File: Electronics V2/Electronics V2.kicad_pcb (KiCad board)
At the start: 2 copper layers, 102 x 62 mm, 88 parts, among them J1 MOT_L, J2 MOT_R, J3 SD_Card, J4 USB_C_Receptacle_USB2.0_14P, J5 Power Probes, J6 L1, J7 L2, Q1 BC547, SW1 BTN_0, SW2 MSTP_SEL, SW3 RST, SW4 BOOT, SW5 BTN_1, SW6 BTN_2, SW7 BTN_3, SW8 INCR_0, U1 NCP1117-3.3_SOT223, U10 TVS1400DRV, U11 TVS1400DRV, U2 TMC2209, U3 ESP32-S3-WROOM-1, U4 DAC081C081CIMK, U5 IMU_L, U6 IMU_R, U7 NCP1117-3.3_SOT223, U8 SSD1036, U9 TMC2209

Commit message: completed pcb fr this time
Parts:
- removed the U5 at (108.6, 78.3)
- added U5: IMU_L, Package_LGA:Bosch_LGA-14_3x2.5mm_P0.5mm, F.Cu at (112.7, 92.5)
- added U5: IMU_L, Package_LGA:Bosch_LGA-14_3x2.5mm_P0.5mm, F.Cu at (199.8, 104.2)
- moved U6 52.6 mm to (150.8, 104.4), turned to -90 degrees
- moved 10k 6.82 mm to (194.5, 75.9), turned to 0 degrees
- moved 10n 3.91 mm to (194.5, 74.4), turned to 180 degrees
- moved J4 2.51 mm to (199.7, 113.0)
- moved 10k 1.49 mm to (194.5, 72.9), turned to 180 degrees
- moved J3 0.41 mm to (117.0, 99.6)
- moved 100n 0.38 mm to (158.9, 121.7)
- moved 1k 0.38 mm to (158.8, 119.9)
- moved D1 0.38 mm to (158.9, 118.2)
- moved 10k 0.30 mm to (146.2, 81.0)
- moved 100n 0.18 mm to (197.5, 80.8)
- moved 100n 0.15 mm to (197.5, 82.3)
- moved 10k 0.10 mm to (149.6, 81.0)
- renumbered R24 to 1.5k, C3 to 100n, C11 to 100n, C24 to 100n, C6 to 100n, C17 to 100n, C14 to 100n, C13 to 100n, C5 to 100n, C16 to 100n, C12 to 100n, C7 to 100n, C1 to 100n, C18 to 100n, C10 to 100n, C23 to 100n, C2 to 100n, C4 to 100u, R2 to 10k, R19 to 10k, R1 to 10k, R15 to 10k, R14 to 10k, R9 to 10k, R11 to 10k, R6 to 10k, R16 to 10k, R26 to 10k, R18 to 10k, R25 to 10k, R17 to 10k, R13 to 10k, R7 to 10k, R3 to 10k, R10 to 10k, C26 to 10n, C27 to 10n, C22 to 10u, C19 to 10u, C21 to 10u, C20 to 10u, R23 to 1k, R12 to 1k, R21 to 1k, R22 to 1k, C8 to 22n, C25 to 22n, R8 to 330m, R4 to 330m, R20 to 330m, R5 to 330m, U9 to TMC2209
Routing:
- net GND: track 51.3 -> 9.29 mm, vias 16 -> 0
- net /SCL: track 163.6 -> 140.9 mm, vias 8 -> 7
- net /SDA: track 155.4 -> 141.2 mm, vias 6 -> 7
- net /MISO: track 10.8 -> 4.26 mm
- net Net-(C26-Pad1): track 5.40 -> 9.37 mm
- net /D+: track 46.2 -> 43.7 mm
- net /D-: track 46.2 -> 43.7 mm
- net /VREF: track 53.3 -> 51.3 mm
- net Net-(C27-Pad1): track 12.0 -> 10.5 mm, vias 2 -> 0
- net /CS_SD: track 31.4 -> 32.8 mm
- net +5V: track 211.1 -> 209.9 mm
- net /SCLK: track 13.6 -> 14.7 mm
- net /~{EN}: track 68.5 -> 67.5 mm
- net /MOSI: track 28.0 -> 27.1 mm
- net /DIR_L: track 37.5 -> 36.6 mm
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- removed copper zone on B.Cu, net GND
- removed copper zone on F.Cu, net GND

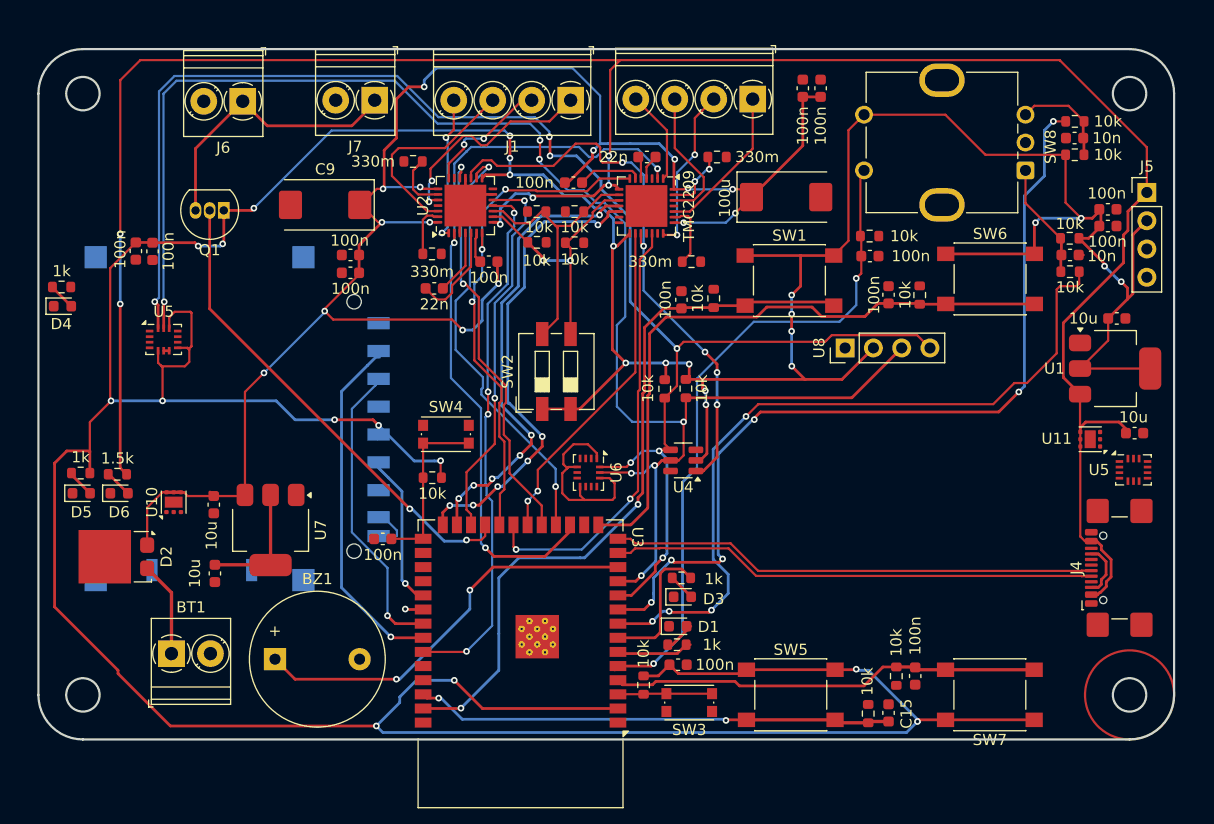
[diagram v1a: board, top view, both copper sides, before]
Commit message: added copper fill
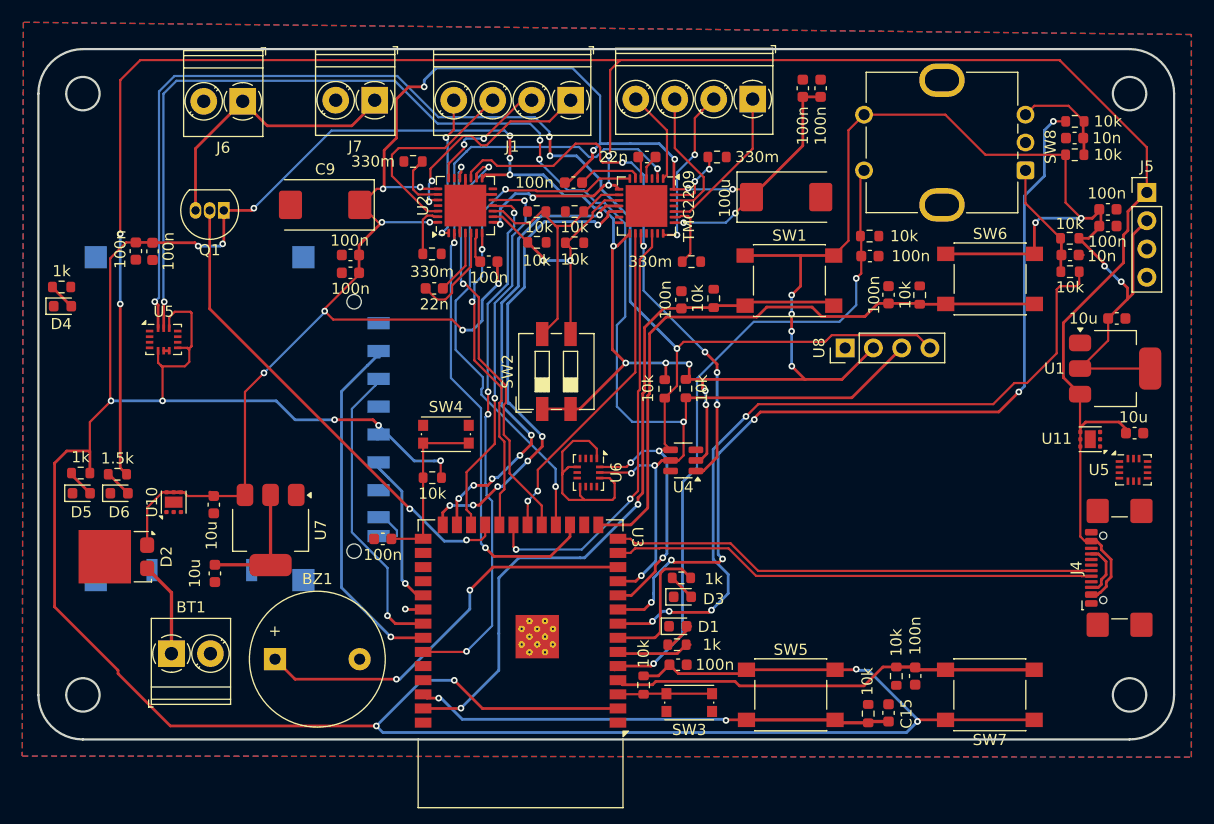
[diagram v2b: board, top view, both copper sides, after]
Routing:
- net +3V3: track 482.3 -> 483.7 mm
- added copper zone on B.Cu, net GND
- added copper zone on F.Cu, net GND

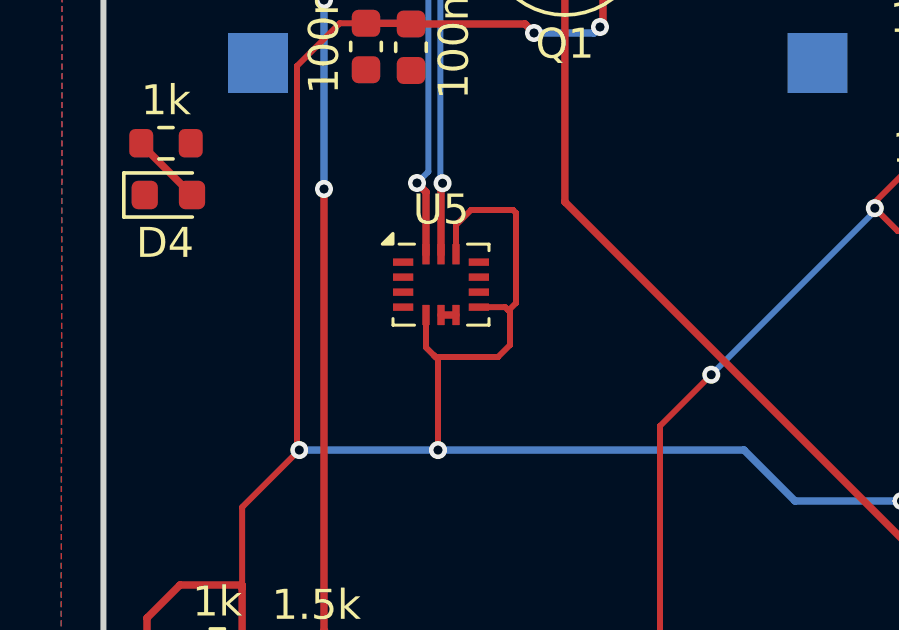
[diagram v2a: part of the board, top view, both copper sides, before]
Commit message: added copper fill + cleaning
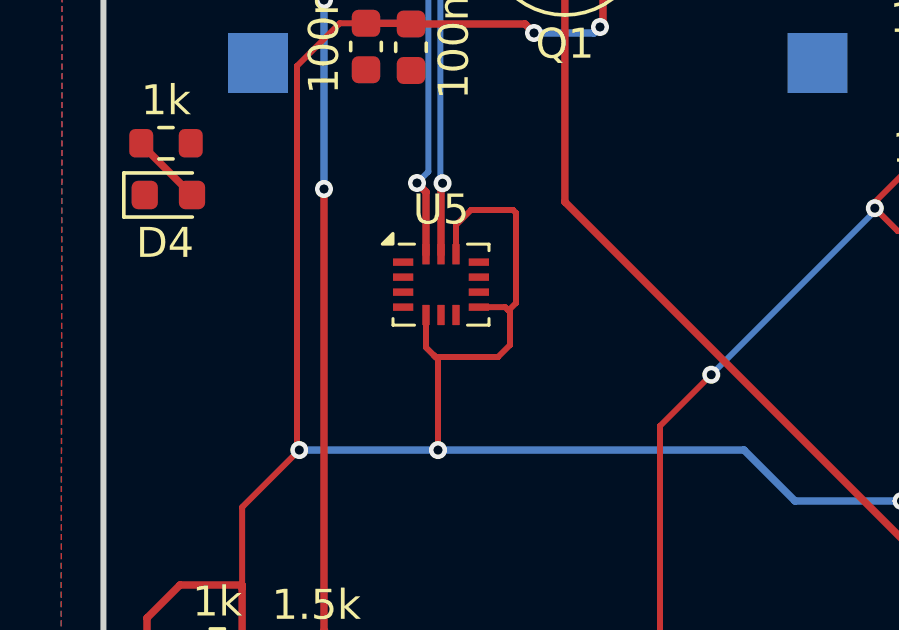
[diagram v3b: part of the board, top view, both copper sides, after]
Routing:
- net GND: track 9.29 -> 8.79 mm
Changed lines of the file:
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@@
-	)
-	(segment
-		(start 113.2 93.5)
-		(end 112.7 93.5)
-		(width 0.25)
-		(layer "F.Cu")
-		(net 2)
 	)
 	(segment

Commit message: branch
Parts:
- removed 1.5k: 1.5k, Resistor_SMD:R_0603_1608Metric
- removed 100n (x16): 100n, Capacitor_SMD:C_0603_1608Metric
- removed 100u: 100u, Capacitor_Tantalum_SMD:CP_EIA-7343-30_AVX-N
- removed 10k (x17): 10k, Resistor_SMD:R_0603_1608Metric
- removed 10n (x2): 10n, Capacitor_SMD:C_0603_1608Metric
- removed 10u (x4): 10u, Capacitor_SMD:C_0603_1608Metric
- removed 1k (x4): 1k, Resistor_SMD:R_0603_1608Metric
- removed 22n (x2): 22n, Capacitor_SMD:C_0603_1608Metric
- removed 330m (x4): 330m, Resistor_SMD:R_0603_1608Metric
- removed TMC2209: TMC2209, Package_DFN_QFN:QFN-28-1EP_5x5mm_P0.5mm_EP3.75x3.75mm
- removed the U5 at (112.7, 92.5)
- removed the U5 at (199.8, 104.2)
- added C1: 100n, Capacitor_SMD:C_0603_1608Metric, F.Cu at (43.5, 104.9)
- added C10: 100n, Capacitor_SMD:C_0603_1608Metric, F.Cu at (79.2, 65.5)
- added C11: 100n, Capacitor_SMD:C_0603_1608Metric, F.Cu at (43.5, 112.5)
- added C12: 100n, Capacitor_SMD:C_0603_1608Metric, F.Cu at (43.5, 115.0)
- added C13: 100n, Capacitor_SMD:C_0603_1608Metric, F.Cu at (43.5, 117.5)
- added C14: 100n, Capacitor_SMD:C_0603_1608Metric, F.Cu at (43.5, 120.0)
- added C16: 100n, Capacitor_SMD:C_0603_1608Metric, F.Cu at (47.5, 107.4)
- added C17: 100n, Capacitor_SMD:C_0603_1608Metric, F.Cu at (47.5, 110.0)
- added C18: 100n, Capacitor_SMD:C_0603_1608Metric, F.Cu at (47.5, 112.5)
- added C19: 10u, Capacitor_SMD:C_0603_1608Metric, F.Cu at (47.5, 115.0)
- added C2: 100n, Capacitor_SMD:C_0603_1608Metric, F.Cu at (43.5, 107.4)
- added C20: 10u, Capacitor_SMD:C_0603_1608Metric, F.Cu at (47.5, 117.5)
- added C21: 10u, Capacitor_SMD:C_0603_1608Metric, F.Cu at (47.5, 120.0)
- added C22: 10u, Capacitor_SMD:C_0603_1608Metric, F.Cu at (51.5, 104.9)
- added C23: 100n, Capacitor_SMD:C_0603_1608Metric, F.Cu at (79.2, 68.0)
- added C24: 100n, Capacitor_SMD:C_0603_1608Metric, F.Cu at (79.2, 70.5)
- added C25: 22n, Capacitor_SMD:C_0603_1608Metric, F.Cu at (79.2, 73.0)
- added C26: 10n, Capacitor_SMD:C_0603_1608Metric, F.Cu at (51.5, 107.4)
- added C27: 10n, Capacitor_SMD:C_0603_1608Metric, F.Cu at (51.5, 110.0)
- added C3: 100n, Capacitor_SMD:C_0603_1608Metric, F.Cu at (43.5, 110.0)
- added C4: 100u, Capacitor_Tantalum_SMD:CP_EIA-7343-30_AVX-N, F.Cu at (86.2, 45.0)
- added C5: 100n, Capacitor_SMD:C_0603_1608Metric, F.Cu at (79.2, 43.4)
- added C6: 100n, Capacitor_SMD:C_0603_1608Metric, F.Cu at (79.2, 45.9)
- added C7: 100n, Capacitor_SMD:C_0603_1608Metric, F.Cu at (79.2, 48.4)
- added C8: 22n, Capacitor_SMD:C_0603_1608Metric, F.Cu at (79.2, 50.9)
- added R1: 10k, Resistor_SMD:R_0603_1608Metric, F.Cu at (51.5, 112.5)
- added R10: 10k, Resistor_SMD:R_0603_1608Metric, F.Cu at (51.5, 117.5)
- added R11: 10k, Resistor_SMD:R_0603_1608Metric, F.Cu at (51.5, 120.0)
- added R12: 1k, Resistor_SMD:R_0603_1608Metric, F.Cu at (55.5, 104.9)
- added R13: 10k, Resistor_SMD:R_0603_1608Metric, F.Cu at (55.5, 107.4)
- added R14: 10k, Resistor_SMD:R_0603_1608Metric, F.Cu at (55.5, 110.0)
- added R15: 10k, Resistor_SMD:R_0603_1608Metric, F.Cu at (55.5, 112.5)
- added R16: 10k, Resistor_SMD:R_0603_1608Metric, F.Cu at (55.5, 115.0)
- added R17: 10k, Resistor_SMD:R_0603_1608Metric, F.Cu at (55.5, 117.5)
- added R18: 10k, Resistor_SMD:R_0603_1608Metric, F.Cu at (55.5, 120.0)
- added R19: 10k, Resistor_SMD:R_0603_1608Metric, F.Cu at (59.5, 104.9)
- added R2: 10k, Resistor_SMD:R_0603_1608Metric, F.Cu at (79.2, 53.4)
- added R20: 330m, Resistor_SMD:R_0603_1608Metric, F.Cu at (79.2, 83.0)
- added R21: 1k, Resistor_SMD:R_0603_1608Metric, F.Cu at (59.5, 107.4)
- added R22: 1k, Resistor_SMD:R_0603_1608Metric, F.Cu at (59.5, 110.0)
- added R23: 1k, Resistor_SMD:R_0603_1608Metric, F.Cu at (59.5, 112.5)
- added R24: 1.5k, Resistor_SMD:R_0603_1608Metric, F.Cu at (59.5, 115.0)
- added R25: 10k, Resistor_SMD:R_0603_1608Metric, F.Cu at (59.5, 117.5)
- added R26: 10k, Resistor_SMD:R_0603_1608Metric, F.Cu at (59.5, 120.0)
- added R3: 10k, Resistor_SMD:R_0603_1608Metric, F.Cu at (79.2, 55.9)
- added R4: 330m, Resistor_SMD:R_0603_1608Metric, F.Cu at (79.2, 58.4)
- added R5: 330m, Resistor_SMD:R_0603_1608Metric, F.Cu at (79.2, 61.0)
- added R6: 10k, Resistor_SMD:R_0603_1608Metric, F.Cu at (79.2, 75.5)
- added R7: 10k, Resistor_SMD:R_0603_1608Metric, F.Cu at (79.2, 78.0)
- added R8: 330m, Resistor_SMD:R_0603_1608Metric, F.Cu at (79.2, 80.5)
- added R9: 10k, Resistor_SMD:R_0603_1608Metric, F.Cu at (51.5, 115.0)
- added U5: IMU_L, Package_LGA:Bosch_LGA-14_3x2.5mm_P0.5mm, F.Cu at (125.2, 124.0)
- added U9: TMC2209, Package_DFN_QFN:QFN-28-1EP_5x5mm_P0.5mm_EP3.75x3.75mm, F.Cu at (180.0, 85.7)
- moved J5 139.2 mm to (66.2, 44.5)
- moved U11 132.3 mm to (65.2, 80.8), turned to 0 degrees
- moved U1 132.3 mm to (66.5, 107.9)
- moved C15 132.0 mm to (47.5, 104.9), turned to 0 degrees
- moved D1 122.5 mm to (61.9, 43.4)
- moved D3 119.7 mm to (61.9, 46.0)
- moved SW3 117.0 mm to (64.1, 58.0), turned to 0 degrees
- moved BZ1 103.0 mm to (49.3, 48.9)
- moved SW2 91.5 mm to (57.9, 79.5), turned to 0 degrees
- moved BT1 87.9 mm to (196.6, 92.2), turned to 90 degrees
- moved SW4 83.3 mm to (64.1, 62.6)
- moved U6 76.6 mm to (226.4, 116.5), turned to 0 degrees
- moved D6 70.3 mm to (61.9, 53.8)
- moved D5 70.1 mm to (61.9, 51.2)
- moved SW5 68.4 mm to (104.1, 102.9), turned to 90 degrees
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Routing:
- net +3V3: track 483.7 -> 0.00 mm, vias 29 -> 0
- net +5V: track 209.9 -> 0.00 mm, vias 6 -> 0
- net VBAT: track 157.1 -> 0.00 mm, vias 15 -> 0
- net /SDA: track 141.2 -> 0.00 mm, vias 7 -> 0
- net /SCL: track 140.9 -> 0.00 mm, vias 7 -> 0
- net /INCR_B: track 78.3 -> 0.00 mm, vias 6 -> 0
- net /INCR_A: track 68.2 -> 0.00 mm, vias 4 -> 0
- net /~{EN}: track 67.7 -> 0.00 mm, vias 3 -> 0
- net /BTN_0: track 66.0 -> 0.00 mm, vias 2 -> 0
- net /INCR_BTN: track 61.1 -> 0.00 mm, vias 2 -> 0
- net /BTN_2: track 57.2 -> 0.00 mm
- net /VREF: track 51.3 -> 0.00 mm, vias 5 -> 0
- net /DIAG_L: track 48.1 -> 0.00 mm, vias 4 -> 0
- net /SPREAD: track 46.2 -> 0.00 mm, vias 3 -> 0
- net /D-: track 43.7 -> 0.00 mm
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- removed copper zone on B.Cu, net GND
- removed copper zone on F.Cu, net GND
